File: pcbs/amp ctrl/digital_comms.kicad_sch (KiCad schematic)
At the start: 53 parts

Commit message: Schematic file fix, misc. PCB
Fixed issue with KiCAD's automatic V5→V6 migration (corrected in 6.0.11) that caused problems with component references in multi-channel schematic sheets
Finished migration in amp ctrl PCB, inc. re-assigning "exclude from BOM" attributes to testpoints, solder jumpers
Added mounting hole to amp ctrl PCB for addl support to Ethernet jacks, power connector through stiffener
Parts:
- gave numbers to parts that had none: 51

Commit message: New CS amp, misc. layout
Changed current sense amp from INA828 to INA821/819 due to availability: schematic, layout for channel 1 (#6)
Moved some thermistor components & ~Shutdown cap out of the way of the stiffener (#3)
Updated footprints: SOD-323F for slightly larger solderable pads, SOIC-8 to remove excessive length on inside edge
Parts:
- U62, U63, U71: footprint Martinos_std:SOIC-8_3.9x4.9mm_P1.27mm -> Don_std:SOIC-8_3.9x4.9mm_P1.27mm
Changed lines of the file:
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@@
     (property "Reference" "U62" (id 0) (at 251.46 115.57 0))
     (property "Value" "FIN1028" (id 1) (at 254 118.11 0))
-    (property "Footprint" "Martinos_std:SOIC-8_3.9x4.9mm_P1.27mm" (id 2) (at 284.48 153.67 0)
+    (property "Footprint" "Don_std:SOIC-8_3.9x4.9mm_P1.27mm" (id 2) (at 284.48 153.67 0)
       (effects (font (size 1.27 1.27)) hide)
     )
@@
     (property "Reference" "U63" (id 0) (at 251.46 161.29 0))
     (property "Value" "FIN1028" (id 1) (at 254 163.83 0))
-    (property "Footprint" "Martinos_std:SOIC-8_3.9x4.9mm_P1.27mm" (id 2) (at 284.48 199.39 0)
+    (property "Footprint" "Don_std:SOIC-8_3.9x4.9mm_P1.27mm" (id 2) (at 284.48 199.39 0)
       (effects (font (size 1.27 1.27)) hide)
     )
@@
     (property "Reference" "U71" (id 0) (at 251.46 220.98 0))
     (property "Value" "FIN1028" (id 1) (at 254 223.52 0))
-    (property "Footprint" "Martinos_std:SOIC-8_3.9x4.9mm_P1.27mm" (id 2) (at 284.48 259.08 0)
-      (effects (font (size 1.27 1.27)) hide)
-    )
+    (property "Footprint" "Don_std:SOIC-8_3.9x4.9mm_P1.27mm" (id 2) (at 284.48 259.08 0)
+      (effects (font (size 1.27 1.27)) hide)
+    )

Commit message: New DAC
Changed DAC from LTC2656 to AD5676 (#5)
Changed digital Vdd for ADC to +3.3V
Removed level translator ICs for +3.3V to +5V; no longer needed because AD5676 has separate analog and digital supply pins
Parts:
- removed C202, C203, C204: 100nF 50V X7R, Capacitor_SMD:C_0603_1608Metric, symbol Device:C
- removed U65, U66: 74LVC2T45, Martinos_std:VSSOP-8_2.3x2mm_P0.5mm, symbol Logic_LevelTranslator:74LVC2T45DC
- added JP71: Jumper_2_Bridged, Jumper:SolderJumper-2_P1.3mm_Bridged_RoundedPad1.0x1.5mm, symbol Jumper:Jumper_2_Bridged
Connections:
- net +5V is gone; now on net +3V3: C254.2, C255.2, C256.2, U47.5 (VCC)
- net ADC_MISO: now also U64.7 (DIN4)
- net DAC_MISO: now also U64.3 (DIN2)
- net SCKI: now also JP71.1 (A)
- net SCKO: now also JP71.2 (B)
- no-connect marks 18 -> 17
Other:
- note removed: "Delay typ. 3 ns or less, max. 5 ns"
- note removed: "SCKI doesn't need level translation, but adds delay to SCKO signal to match the delay added to MISO signals by level shifter so that the clock and data signals remain better-aligned"

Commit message: Upgraded to KiCAD 7.0 format Added 10µF cap to ADC's REFP pins to fix the voltage reference output (#15) Corrected ADC & DAC reset by adding a separate reset circuit (#14) Increased Cfbk compensation cap on each channel to work out-of-the-box with small coils (#16)
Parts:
- added C204: 1nF 50V NP0, Capacitor_SMD:C_0603_1608Metric, symbol Device:C
- added R289: 10K, Resistor_SMD:R_0805_2012Metric, symbol Device:R
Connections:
- net +3V3: now also R289.2
- net GND: now also C204.1; no longer U47.3
- net ~{Reset}: now also U47.4; no longer R287.2, U47.6
- new net: R287.2, U47.6
- new net: C204.2, R289.1, U47.3
- no-connect marks 17 -> 16
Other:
- note added: "A"
- note added: "B"
- note added: "C"
- note removed: "* LVDS transceiver output levels are LVTTL (compatible with 3.3V CMOS), same as ADC/DAC inputs despite different supply voltages * LVDS transceiver inputs can only tolerate 3.3V +1V though, and ADC/DAC outputs are 5V CMOS, so both MISO signals need level translation"
- note removed: "Power-on shutdown: Holds all channels in shutdown for ~500 ms at power-up, to give time for Vmid to settle and avoid output current spikes; also used to reset ADC"
- moved on the sheet: C254, C255, C256, R285, U47A, U47B

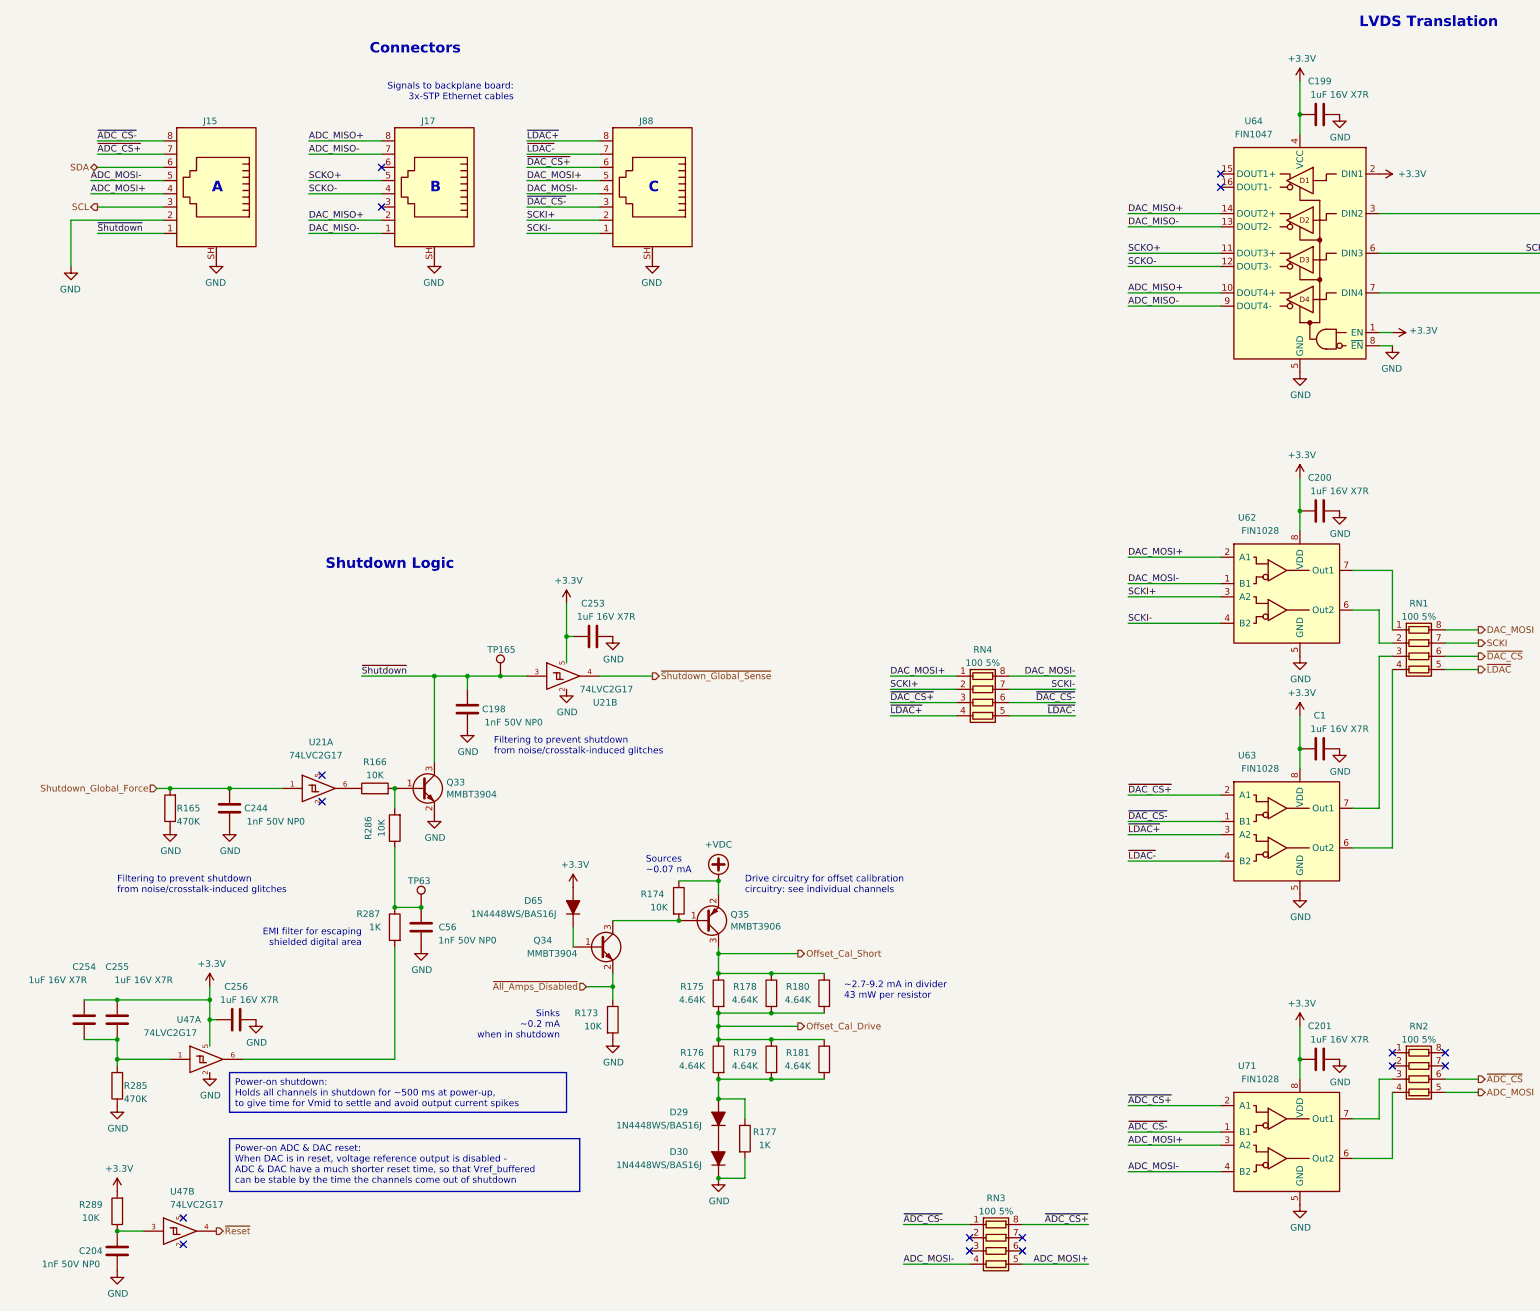
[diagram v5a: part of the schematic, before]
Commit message: Amp ctrl: lengthened ADC & DAC reset delay to ~50 ms (#14) Backplane: added clock multiplier for 10 Mhz scanner clock (fixes #21) Backplane: reduced R5 from 10 to 1 ohm, to avoid excessive voltage drop (#20) Backplane: replaced 15V regulator with efficient voltage limiter (#20) Backplane: changed all mounting holes to signal ground Backplane: replaced +2.5V regulator with a higher-current model to support FPGA I/O bank current draw Updated to KiCAD 8
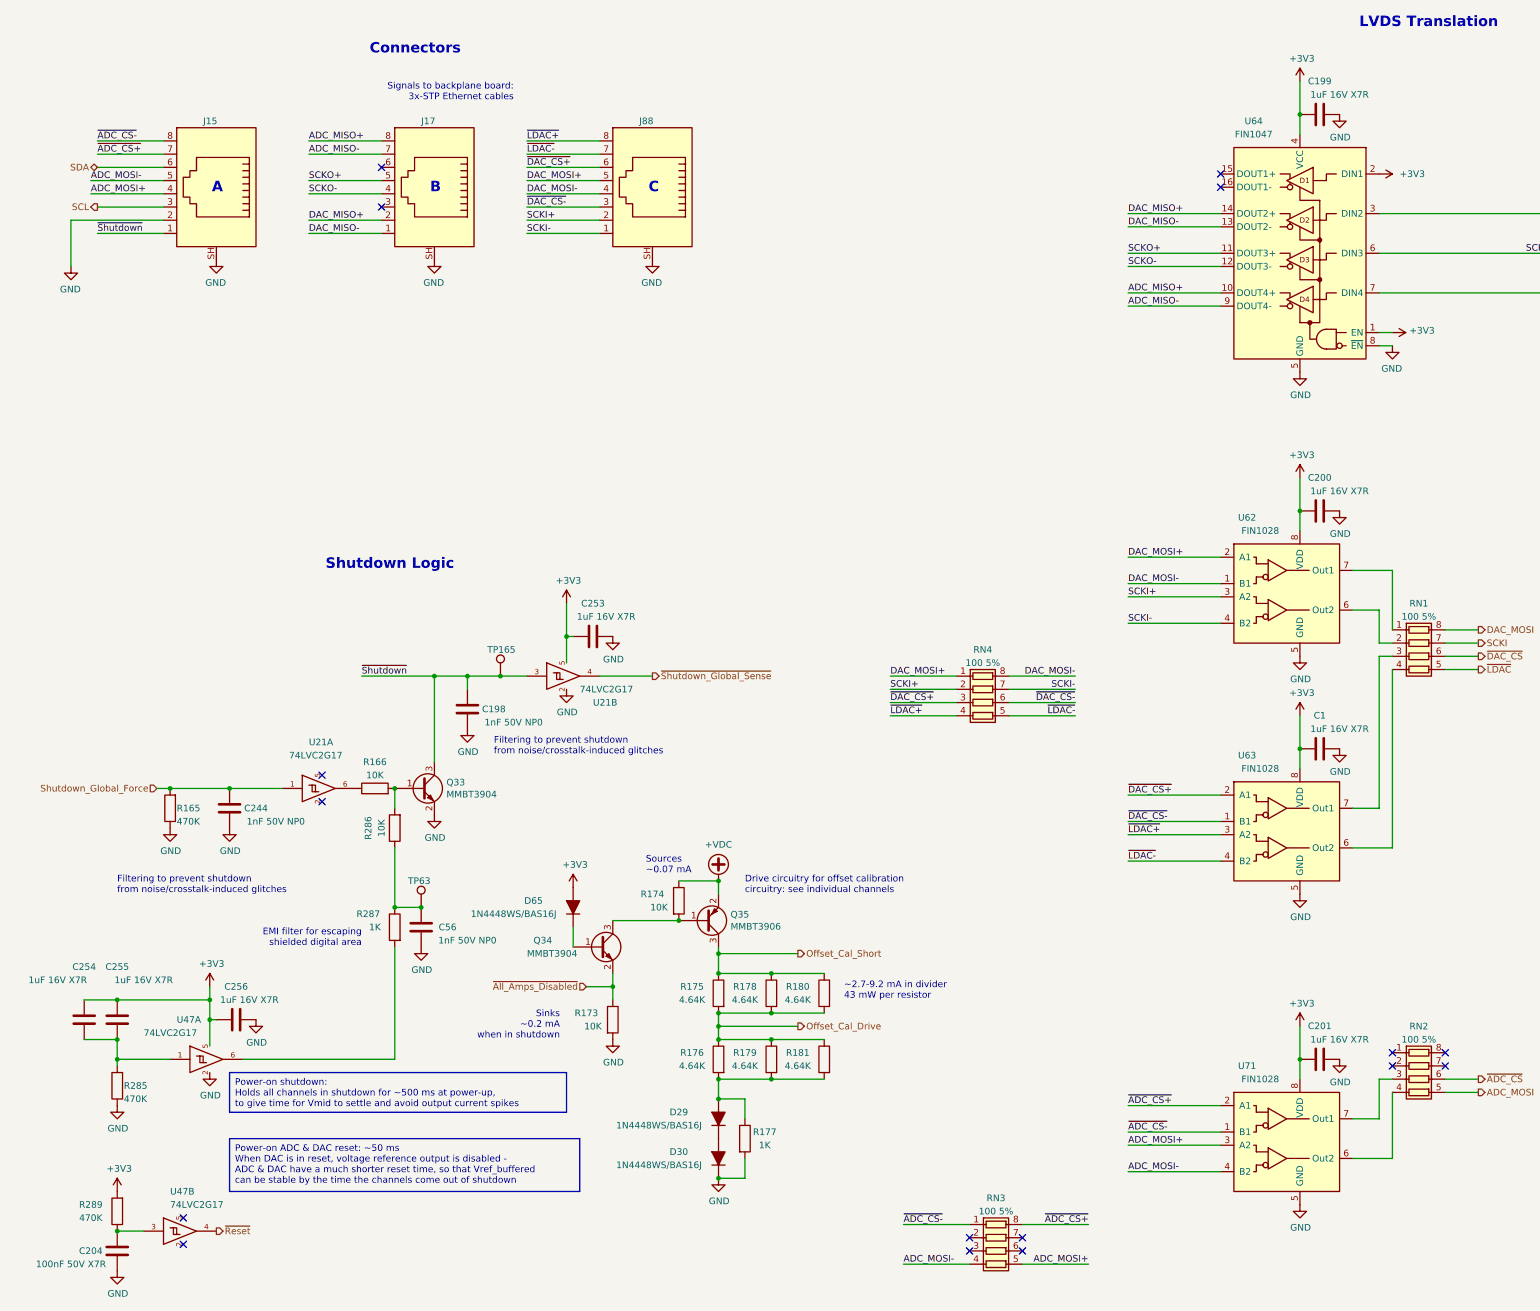
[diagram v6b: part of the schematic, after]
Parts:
- C204: value 1nF 50V NP0 -> 100nF 50V X7R; Part Number C0603C102J5GACTU -> C0603C104K5RACTU
- D29, D30, D65: footprint Martinos_std:D_SOD-323F -> Don_std:D_SOD-323F
- R289: value 10K -> 470K; Part Number RK73H2ATTE1002F -> RK73H2ATTD4703F

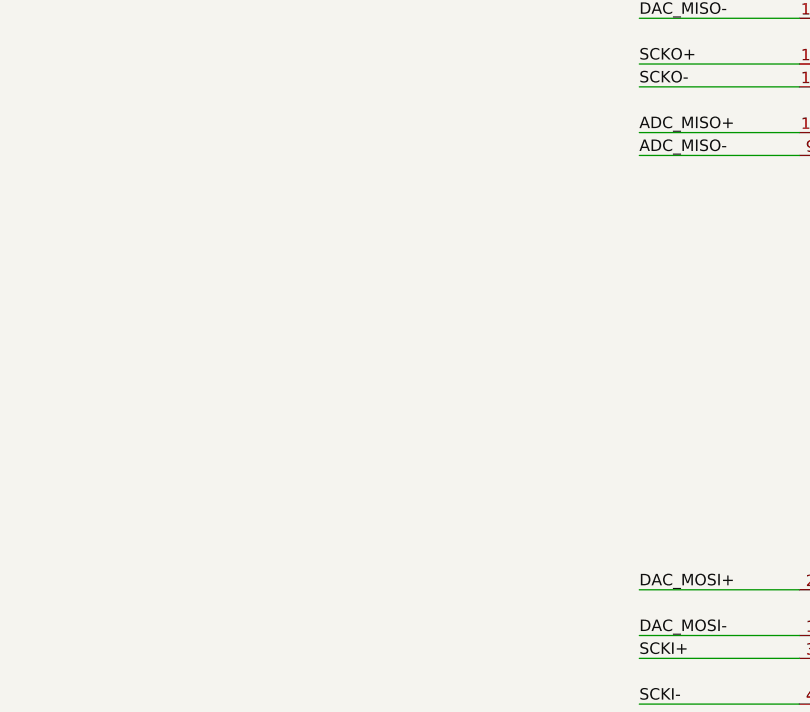
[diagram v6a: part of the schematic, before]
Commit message: Comms fix, misc. improvements
Added 33KΩ pull-ups & pull-downs to amp ctrl board's LVDS inputs, to solve issues caused by unconfigured FPGA pins during boot (fixes #23)
Swapped backplane power input polarity for consistency with power connectors (fixes #20)
Added "manual enable" optical input to backplane, for safety: requires positive enable to keep amplifiers enabled
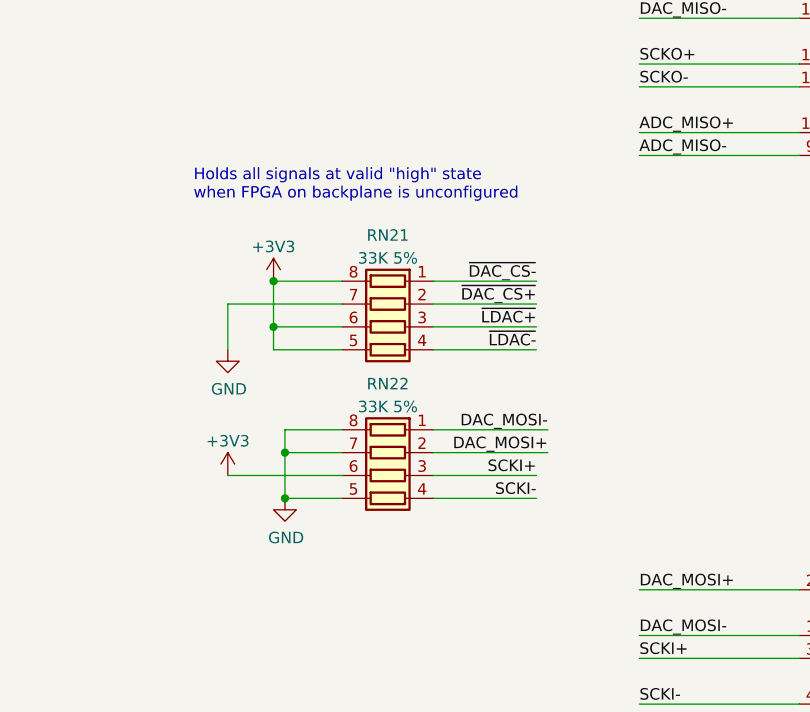
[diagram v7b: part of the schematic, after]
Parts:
- added RN21, RN22: 33K 5%, Don_std:R_Array_Concave_4x0603, symbol Device:R_Pack04
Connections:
- net +3V3: now also RN21.5 (R4.2), RN21.6 (R3.2), RN21.8 (R1.2), RN22.6 (R3.2)
- net DAC_MOSI+: now also RN22.2 (R2.1)
- net DAC_MOSI-: now also RN22.1 (R1.1)
- net GND: now also RN21.7 (R2.2), RN22.5 (R4.2), RN22.7 (R2.2), RN22.8 (R1.2)
- net SCKI+: now also RN22.3 (R3.1)
- net SCKI-: now also RN22.4 (R4.1)
- net ~{DAC_CS+}: now also RN21.2 (R2.1)
- net ~{DAC_CS-}: now also RN21.1 (R1.1)
- net ~{LDAC+}: now also RN21.3 (R3.1)
- net ~{LDAC-}: now also RN21.4 (R4.1)
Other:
- note added: "Holds all signals at valid "high" state when FPGA on backplane is unconfigured"
